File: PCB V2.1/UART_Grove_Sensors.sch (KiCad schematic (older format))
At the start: 11 parts, among them J5 B4B-PH-K-S(LF)(SN), J6 B4B-PH-K-S(LF)(SN), J7 B4B-PH-K-S(LF)(SN), J8 B4B-PH-K-S(LF)(SN), U4 74HC4052D

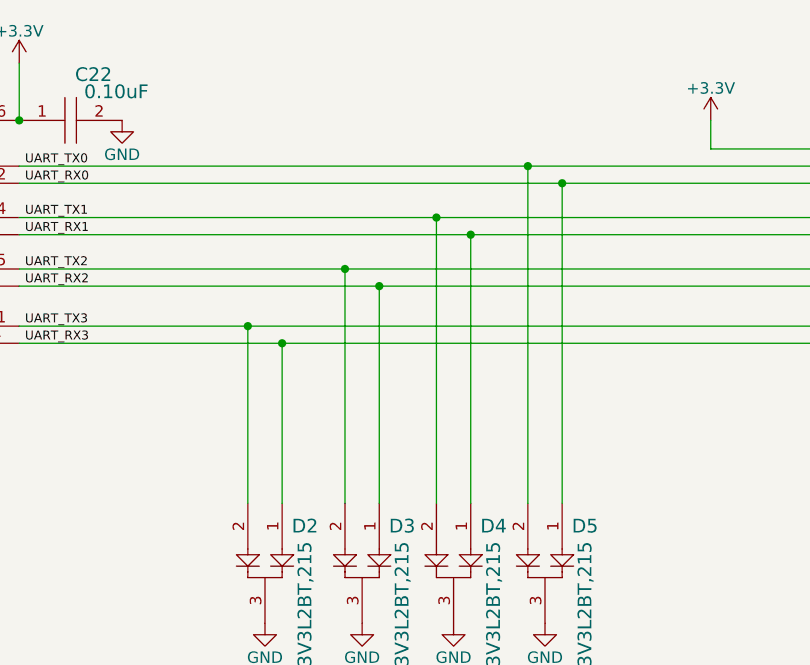
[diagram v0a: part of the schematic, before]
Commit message: Internal Planes
Internal Planes added, small amount of routing left.
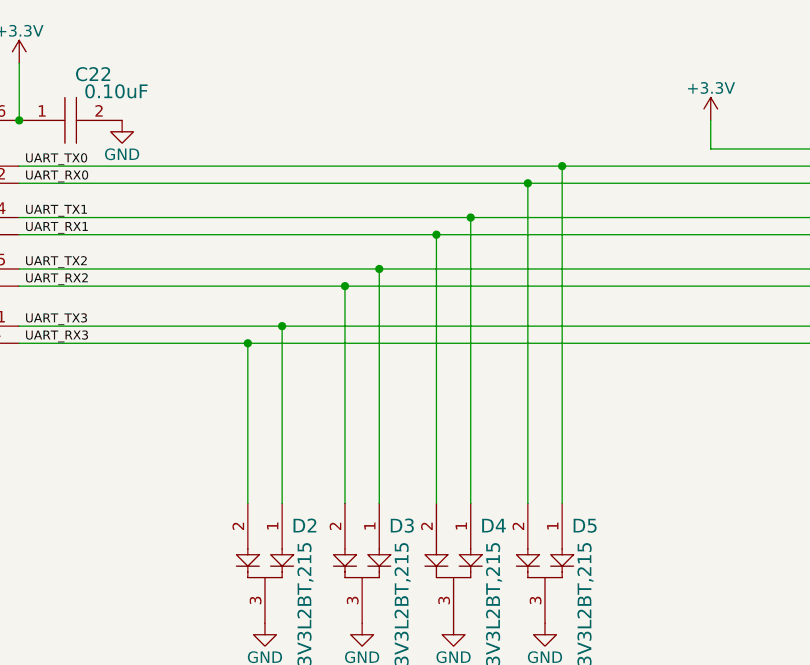
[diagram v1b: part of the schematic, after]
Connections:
- net UART_RX0: now also D5.2; no longer D5.1
- net UART_RX1: now also D4.2; no longer D4.1
- net UART_RX2: now also D3.2; no longer D3.1
- net UART_RX3: now also D2.2; no longer D2.1
- net UART_TX0: now also D5.1; no longer D5.2
- net UART_TX1: now also D4.1; no longer D4.2
- net UART_TX2: now also D3.1; no longer D3.2
- net UART_TX3: now also D2.1; no longer D2.2
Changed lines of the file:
@@
 LIBS:contrib
 LIBS:valves
-LIBS:stm32
-LIBS:ESP8266
 LIBS:HydroPWNics_Lib
 LIBS:ESP32-footprints-Shem-Lib
@@
 Wire Wire Line
 	6400 3850 6875 3850
-Wire Wire Line
-	4525 4700 4525 5400
-Connection ~ 4525 4700
-Wire Wire Line
-	4375 4625 4375 5400
-Connection ~ 4375 4625
-Wire Wire Line
-	4800 5400 4800 4375
-Connection ~ 4800 4375
-Wire Wire Line
-	4950 5400 4950 4450
-Connection ~ 4950 4450
-Wire Wire Line
-	5200 5400 5200 4150
-Connection ~ 5200 4150
-Wire Wire Line
-	5350 5400 5350 4225
-Connection ~ 5350 4225
-Wire Wire Line
-	5600 5400 5600 3925
-Connection ~ 5600 3925
-Wire Wire Line
-	5750 5400 5750 4000
-Connection ~ 5750 4000
+Connection ~ 4375 4700
+Connection ~ 4525 4625
+Connection ~ 4950 4375
+Connection ~ 4800 4450
+Connection ~ 5350 4150
+Connection ~ 5200 4225
+Connection ~ 5750 3925
+Connection ~ 5600 4000
 $Comp
 L GND #PWR41
@@
 Text Label 1125 3975 0    39   ~ 0
 UART_S_RX
+Wire Wire Line
+	5600 4000 5600 5400
+Wire Wire Line
+	5750 3925 5750 5400
+Wire Wire Line
+	5350 4150 5350 5400
+Wire Wire Line
+	5200 5400 5200 4225
+Wire Wire Line
+	4950 4375 4950 5400
+Wire Wire Line
+	4800 5400 4800 4450
+Wire Wire Line
+	4525 4625 4525 5400
+Wire Wire Line
+	4375 4700 4375 5400
 $EndSCHEMATC
